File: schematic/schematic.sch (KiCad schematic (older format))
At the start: 59 parts, among them J1 Switch Pedal Jack, J2 MIDI OUT, J3 MIDI IN, J4 Expression Pedal Jack, SW1 SW_Push, SW2 SW_Push, SW3 SW_Push, SW4 SW_Push, SW5 SW_Push, SW6 SW_Push, SW7 SW_Push, SW8 SW_Push, U1 MCP23017_SP, U2 Teensy-LC, U3 6N138

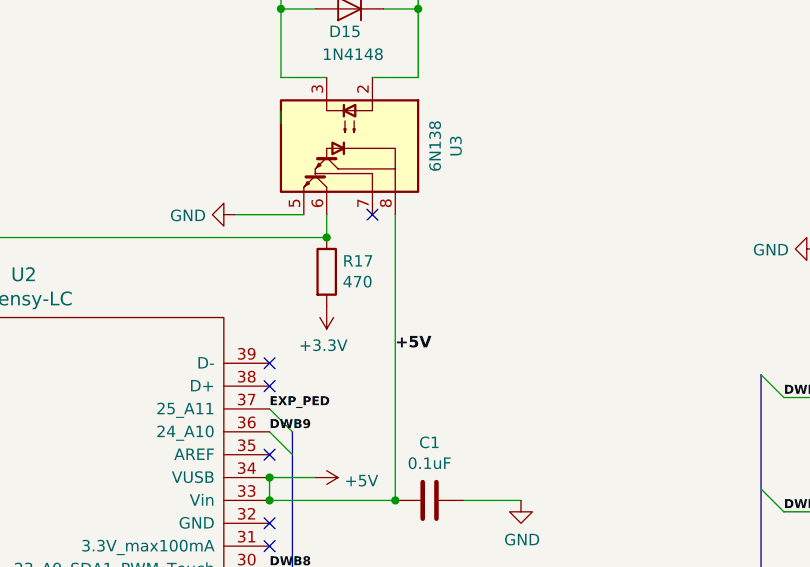
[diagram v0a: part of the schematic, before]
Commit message: Updated with not required resistor to reflect the real perfboard
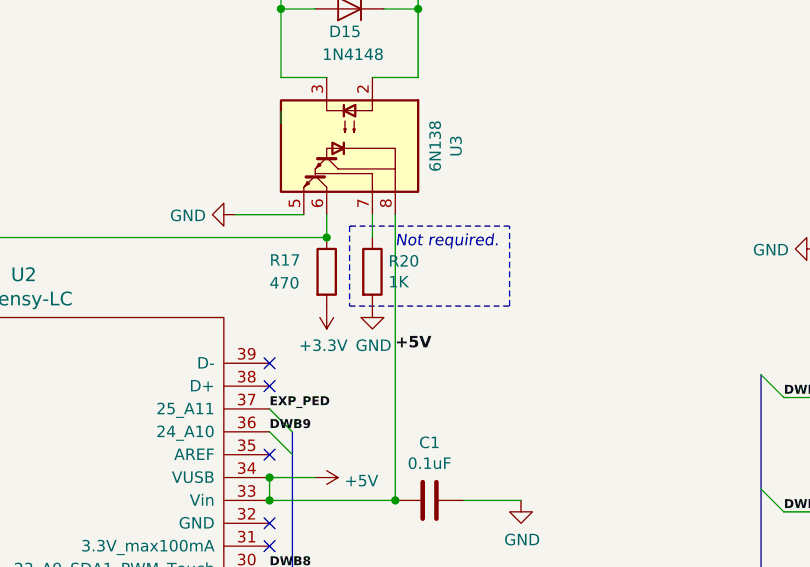
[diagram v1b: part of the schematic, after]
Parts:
- added R20: 1K, symbol Device:R
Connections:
- net GND: now also R20.2
- net at U3.7 (VO1): now also R20.1
- no-connect marks 23 -> 22
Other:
- note added: "Not required."
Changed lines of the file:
@@
 EESchema Schematic File Version 4
+LIBS:schematic-cache
 EELAYER 29 0
 EELAYER END
@@
 U 1 1 5C9A6677
 P 6400 2550
-F 0 "R17" H 6470 2596 50  0000 L CNN
-F 1 "470" H 6470 2505 50  0000 L CNN
+F 0 "R17" H 6150 2600 50  0000 L CNN
+F 1 "470" H 6150 2500 50  0000 L CNN
 F 2 "Resistor_THT:R_Axial_DIN0204_L3.6mm_D1.6mm_P5.08mm_Horizontal" V 6330 2550 50  0001 C CNN
 F 3 "~" H 6400 2550 50  0001 C CNN
@@
 	6150 3150 6250 3250
 NoConn ~ 6150 3350
-NoConn ~ 6600 2300
 NoConn ~ 6150 3750
 $Comp
@@
 Wire Bus Line
 	3350 6800 1850 6800
+$Comp
+L Device:R R20
+U 1 1 5C9BFF99
+P 6600 2550
+F 0 "R20" H 6670 2596 50  0000 L CNN
+F 1 "1K" H 6670 2505 50  0000 L CNN
+F 2 "" V 6530 2550 50  0001 C CNN
+F 3 "~" H 6600 2550 50  0001 C CNN
+	1    6600 2550
+	1    0    0    -1
+$EndComp
+$Comp
+L power:GND #PWR?
+U 1 1 5C9C15DB
+P 6600 2700
+F 0 "#PWR?" H 6600 2450 50  0001 C CNN
+F 1 "GND" H 6605 2527 50  0000 C CNN
+F 2 "" H 6600 2700 50  0001 C CNN
+F 3 "" H 6600 2700 50  0001 C CNN
+	1    6600 2700
+	1    0    0    -1
+$EndComp
+Wire Wire Line
+	6600 2300 6600 2400
+Wire Notes Line
+	6500 2350 6500 2700
+Wire Notes Line
+	7200 2700 7200 2350
+Wire Notes Line
+	7200 2350 6500 2350
+Wire Notes Line
+	6500 2700 7200 2700
 Wire Bus Line
 	1850 3050 1850 3950
@@
 Wire Bus Line
 	3350 5400 3350 6800
+Text Notes 6700 2450 0    50   Italic 0
+Not required.
 $EndSCHEMATC

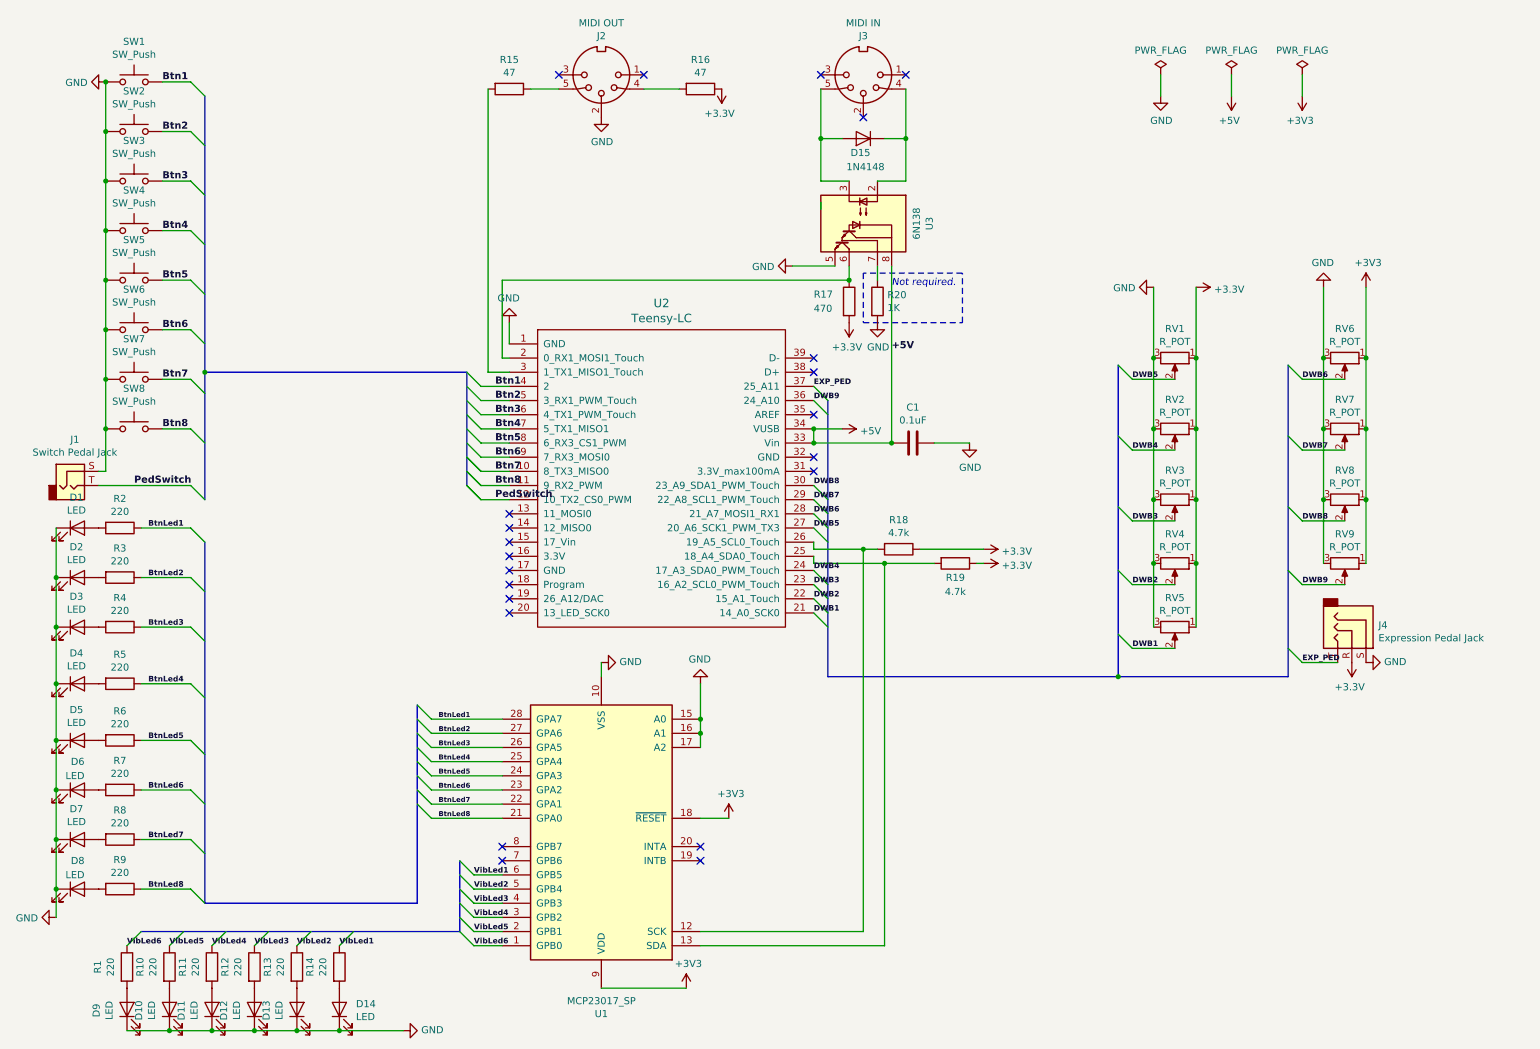
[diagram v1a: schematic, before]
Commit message: New schematic version
With all the connectros and the right pin-connectors order
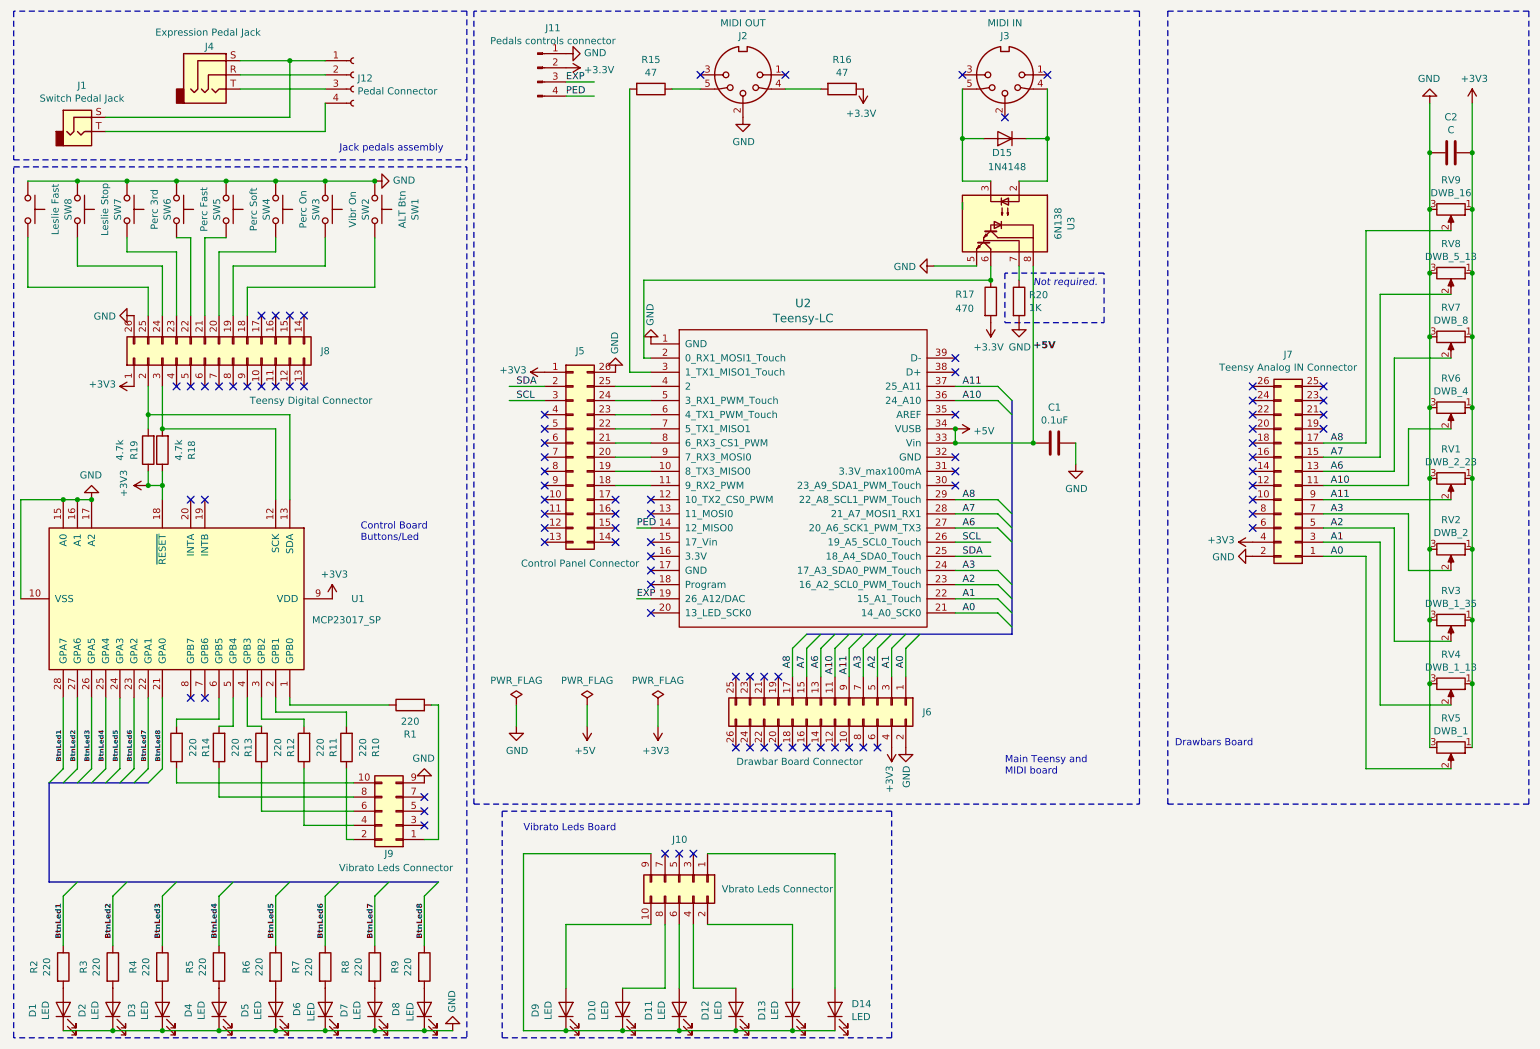
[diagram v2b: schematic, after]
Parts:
- added C2: C, symbol Device:C
- added J10: Vbrato Leds Connector, symbol Connector_Generic:Conn_02x05_Odd_Even
- added J11: Pedals controls connector, symbol Connector:Conn_01x04_Male
- added J12: Pedal Connector, symbol Connector:Conn_01x04_Female
- added J5: Control Panel Connector, symbol Connector_Generic:Conn_02x13_Counter_Clockwise
- added J6: Drawbar Board Connector, symbol Connector_Generic:Conn_02x13_Odd_Even
- added J7: Teensy Analog IN Connector, symbol Connector_Generic:Conn_02x13_Odd_Even
- added J8: Teensy Digital Connector, symbol Connector_Generic:Conn_02x13_Counter_Clockwise
- added J9: Vibrato Leds Connector, symbol Connector_Generic:Conn_02x05_Odd_Even
- RV1: value R_POT -> DWB_2_23
- RV2: value R_POT -> DWB_2
- RV3: value R_POT -> DWB_1_35
- RV4: value R_POT -> DWB_1_13
- RV5: value R_POT -> DWB_1
- RV6: value R_POT -> DWB_4
- RV7: value R_POT -> DWB_8
- RV8: value R_POT -> DWB_5_13
- RV9: value R_POT -> DWB_16
- SW1: value SW_Push -> ALT Btn
- SW2: value SW_Push -> Vibr On
- SW3: value SW_Push -> Perc On
- SW4: value SW_Push -> Perc Soft
- SW5: value SW_Push -> Perc Fast
- SW6: value SW_Push -> Perc 3rd
- SW7: value SW_Push -> Leslie Stop
- SW8: value SW_Push -> Leslie Fast
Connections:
- net labels added: A0, A1, A10, A11, A2, A3, A6, A7, A8, EXP, PED, SCL, SDA
- net labels removed: Btn1, Btn2, Btn3, Btn4, Btn5, Btn6, Btn7, Btn8, DWB1, DWB2, DWB3, DWB4, DWB5, DWB6, DWB7, DWB8, DWB9, EXP_PED, PedSwitch, VibLed1, VibLed2, VibLed3, VibLed4, VibLed5, VibLed6
- wire segments 137 -> 228
- no-connect marks 22 -> 86
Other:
- note added: "Control Board\nButtons/Led"
- note added: "Drawbars Board"
- note added: "Jack pedals assembly"
- note added: "Main Teensy and \nMIDI board"
- note added: "Vibrato Leds Board"
- moved on the sheet: C1, D1, D10, D11, D12, D13, D14, D15, D2, D3, D4, D5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

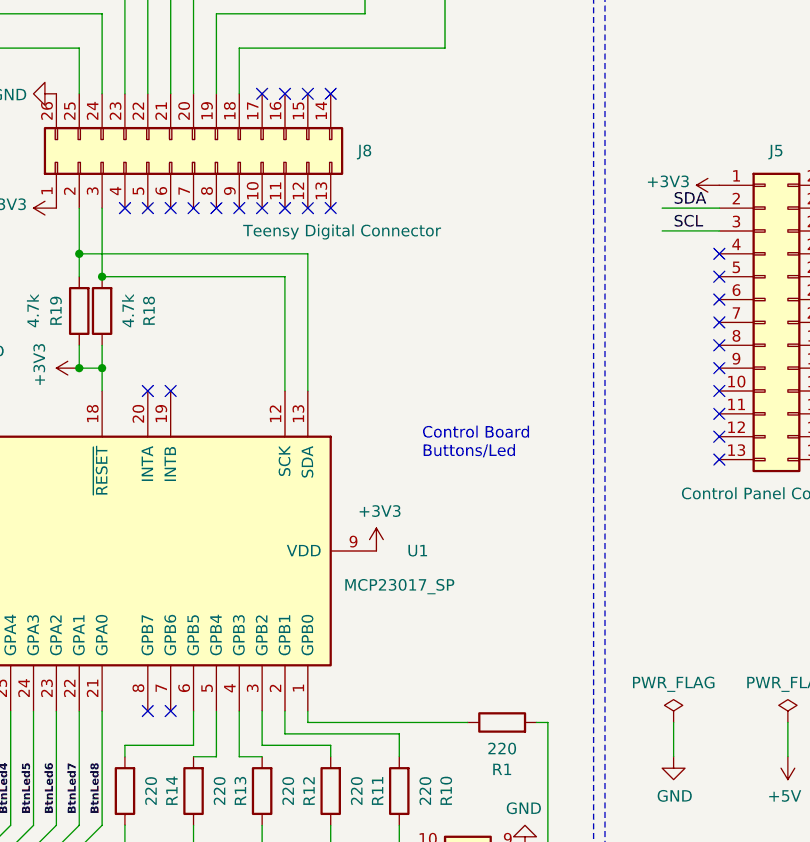
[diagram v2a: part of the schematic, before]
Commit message: adds 24LC64 eeprom
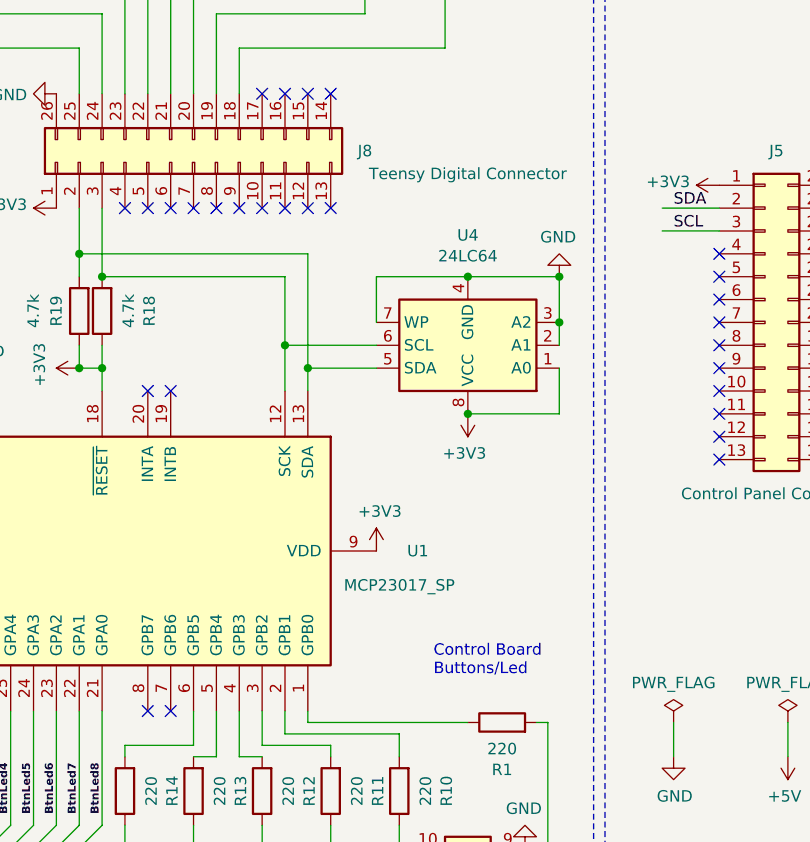
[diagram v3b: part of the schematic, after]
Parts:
- added U4: 24LC64, symbol Memory_EEPROM:24LC64
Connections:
- wire segments 228 -> 239
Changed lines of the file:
@@
 Sheet 1 1
 Title "MIDI Drawbar Commandar"
-Date "2019-04-02"
-Rev "ver. 3.0"
+Date "2020-02-15"
+Rev "ver. 4.0"
 Comp "UBI Stage"
 Comment1 "sgaruti@gmail.com"
-Comment2 ""
+Comment2 "this version adds eeprom memory"
 Comment3 ""
 Comment4 ""
@@
 Wire Wire Line
 	2050 5350 2050 5550
-Wire Wire Line
-	950  3950 1050 3950
-Connection ~ 950  3950
 NoConn ~ 3400 6250
 NoConn ~ 3400 6150
@@
 	-1   0    0    1
 $EndComp
-Connection ~ 850  3950
-Wire Wire Line
-	550  3950 850  3950
-Wire Wire Line
-	850  3950 950  3950
 Wire Wire Line
 	950  5850 950  5350
-$Comp
-L Interface_Expansion:MCP23017_SP U1
-U 1 1 5C8F91DE
-P 1650 4650
-F 0 "U1" V 1650 5931 50  0000 C CNN
-F 1 "MCP23017_SP" V 1800 5850 50  0000 C CNN
-F 2 "Package_DIP:DIP-28_W7.62mm" H 1850 3650 50  0001 L CNN
-F 3 "http://ww1.microchip.com/downloads/en/DeviceDoc/20001952C.pdf" H 1850 3550 50  0001 L CNN
-	1    1650 4650
-	0    1    1    0
-$EndComp
 NoConn ~ 1750 3950
 NoConn ~ 1850 3950
@@
 P 1950 2950
 F 0 "J8" V 2000 2200 50  0000 C CNN
-F 1 "Teensy Digital Connector" V 1650 2300 50  0000 C CNN
+F 1 "Teensy Digital Connector" V 1900 1750 50  0000 C CNN
 F 2 "" H 1950 2950 50  0001 C CNN
 F 3 "~" H 1950 2950 50  0001 C CNN
@@
 Wire Wire Line
 	2450 850  2100 850
-Connection ~ 1050 3950
 Wire Wire Line
 	1550 3950 1550 3850
 Connection ~ 1550 3850
 Wire Wire Line
-	2350 3950 2350 3450
-Wire Wire Line
-	2450 3350 2450 3950
+	2450 3350 2450 3850
 Wire Wire Line
 	3400 6350 3500 6350
@@
 Text Notes 2800 1500 0    50   ~ 0
 Jack pedals assembly
-Text Notes 2950 4250 0    50   ~ 0
+Text Notes 3000 5200 0    50   ~ 0
 Control Board\nButtons/Led
 $Comp
@@
 	1    0    0    -1
 $EndComp
+$Comp
+L power:GND #PWR?
+U 1 1 5CACBC14
+P 5000 2850
+F 0 "#PWR?" H 5000 2600 50  0001 C CNN
+F 1 "GND" V 5005 2722 50  0000 R CNN
+F 2 "" H 5000 2850 50  0001 C CNN
+F 3 "" H 5000 2850 50  0001 C CNN
+	1    5000 2850
+	-1   0    0    1
+$EndComp
+$Comp
+L power:GND #PWR?
+U 1 1 5CACC369
+P 4750 3050
+F 0 "#PWR?" H 4750 2800 50  0001 C CNN
+F 1 "GND" V 4755 2922 50  0000 R CNN
+F 2 "" H 4750 3050 50  0001 C CNN
+F 3 "" H 4750 3050 50  0001 C CNN
+	1    4750 3050
+	-1   0    0    1
+$EndComp
+$Comp
+L Memory_EEPROM:24LC64 U4
+U 1 1 5E48F1C2
+P 3150 3750
+F 0 "U4" H 3150 3269 50  0000 C CNN
+F 1 "24LC64" H 3150 3360 50  0000 C CNN
+F 2 "" H 3150 3750 50  0001 C CNN
+F 3 "http://ww1.microchip.com/downloads/en/DeviceDoc/21189f.pdf" H 3150 3750 50  0001 C CNN
+	1    3150 3750
+	-1   0    0    1
+$EndComp
+Wire Wire Line
+	2350 3950 2350 3750
+Connection ~ 1050 3950
+Wire Wire Line
+	950  3950 1050 3950
+Connection ~ 950  3950
+Wire Wire Line
+	850  3950 950  3950
+Wire Wire Line
+	550  3950 850  3950
+Connection ~ 850  3950
+$Comp
+L Interface_Expansion:MCP23017_SP U1
+U 1 1 5C8F91DE
+P 1650 4650
+F 0 "U1" V 1650 5931 50  0000 C CNN
+F 1 "MCP23017_SP" V 1800 5850 50  0000 C CNN
+F 2 "Package_DIP:DIP-28_W7.62mm" H 1850 3650 50  0001 L CNN
+F 3 "http://ww1.microchip.com/downloads/en/DeviceDoc/20001952C.pdf" H 1850 3550 50  0001 L CNN
+	1    1650 4650
+	0    1    1    0
+$EndComp
+Wire Wire Line
+	2750 3850 2450 3850
+Connection ~ 2450 3850
+Wire Wire Line
+	2450 3850 2450 3950
+Wire Wire Line
+	2750 3750 2350 3750
+Connection ~ 2350 3750
+Wire Wire Line
+	2350 3750 2350 3450
+Wire Wire Line
+	3550 3850 3550 4050
+Wire Wire Line
+	3550 4050 3150 4050
+$Comp
+L power:+3V3 #PWR?
+U 1 1 5E674495
+P 3150 4050
+F 0 "#PWR?" H 3150 3900 50  0001 C CNN
+F 1 "+3V3" H 3165 4223 50  0000 C CNN
+F 2 "" H 3150 4050 50  0001 C CNN
+F 3 "" H 3150 4050 50  0001 C CNN
+	1    3150 4050
+	-1   0    0    1
+$EndComp
+Connection ~ 3150 4050
+Wire Wire Line
+	3550 3750 3550 3650
+Wire Wire Line
+	3550 3450 3150 3450
+Connection ~ 3550 3650
+Wire Wire Line
+	3550 3650 3550 3450
+$Comp
+L power:GND #PWR?
+U 1 1 5E6D20BB
+P 3550 3450
+F 0 "#PWR?" H 3550 3200 50  0001 C CNN
+F 1 "GND" H 3555 3277 50  0000 C CNN
+F 2 "" H 3550 3450 50  0001 C CNN
+F 3 "" H 3550 3450 50  0001 C CNN
+	1    3550 3450
+	-1   0    0    1
+$EndComp
+Connection ~ 3550 3450
+Wire Wire Line
+	2750 3650 2750 3450
+Wire Wire Line
+	2750 3450 3150 3450
 Wire Bus Line
 	750  5950 1450 5950
@@
 Wire Bus Line
 	6100 4900 7550 4900
-$Comp
-L power:GND #PWR?
-U 1 1 5CACBC14
-P 5000 2850
-F 0 "#PWR?" H 5000 2600 50  0001 C CNN
-F 1 "GND" V 5005 2722 50  0000 R CNN
-F 2 "" H 5000 2850 50  0001 C CNN
-F 3 "" H 5000 2850 50  0001 C CNN
-	1    5000 2850
-	-1   0    0    1
-$EndComp
-$Comp
-L power:GND #PWR?
-U 1 1 5CACC369
-P 4750 3050
-F 0 "#PWR?" H 4750 2800 50  0001 C CNN
-F 1 "GND" V 4755 2922 50  0000 R CNN
-F 2 "" H 4750 3050 50  0001 C CNN
-F 3 "" H 4750 3050 50  0001 C CNN
-	1    4750 3050
-	-1   0    0    1
-$EndComp
+Connection ~ 3150 3450
 $EndSCHEMATC
